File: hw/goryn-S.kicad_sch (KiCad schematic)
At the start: 2 parts, among them J2 Conn_01x34

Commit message: added DC-DC
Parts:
- added C8, C9: 22uF, AI6YP:C_0603_1608Metric, symbol AI6YP:C
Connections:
- net +3V3: now also C8.1, C9.1
- net GND: now also C8.2, C9.2
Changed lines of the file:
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@@
+    (stroke (width 0) (type default))
+  )
+  (wire (pts (xy 140 72) (xy 140 74))
     (stroke (width 0) (type default))
   )
@@
     (stroke (width 0) (type default))
   )
+  (wire (pts (xy 130 211) (xy 130 214))
+    (stroke (width 0) (type default))
+  )
   (wire (pts (xy 142 168) (xy 119 168))
     (stroke (width 0) (type default))
   )
+  (wire (pts (xy 130 216) (xy 130 218))
+    (stroke (width 0) (type default))
+  )
   (wire (pts (xy 113 136) (xy 113 132))
     (stroke (width 0) (type default))
@@
     (stroke (width 0) (type default))
   )
+  (wire (pts (xy 140 67) (xy 140 70))
+    (stroke (width 0) (type default))
+  )
   (wire (pts (xy 113 160) (xy 100 160))
     (stroke (width 0) (type default))
@@
     )
   )
+  (symbol (lib_id "AI6YP:C") (at 130 215 0) (unit 1)
+    (in_bom yes) (on_board yes) (dnp no)
+    (property "Reference" "C9" (at 131 214 0)
+      (effects (font (size 1 1)) (justify left))
+    )
+    (property "Value" "22uF" (at 131 216 0)
+      (effects (font (size 1 1)) (justify left))
+    )
+    (property "Footprint" "AI6YP:C_0603_1608Metric" (at 131 219 0)
+      (effects (font (size 1 1)) hide)
+    )
+    (property "Datasheet" "~" (at 130 215 0)
+      (effects (font (size 1 1)) hide)
+    )
+    (pin "1")
+    (pin "2")
+    (instances
+      (project "goryn"
+        (path "/745fe258-3c32-4527-ad01-ef9d3fd5a8f9/ce95a81f-e5e2-402d-b8f8-c902f6a2df69"
+          (reference "C9") (unit 1)
+        )
+      )
+    )
+  )
   (symbol (lib_id "AI6YP:GND") (at 103 116 90) (unit 1)
     (in_bom yes) (on_board yes) (dnp no) (fields_autoplaced)
@@
     )
   )
+  (symbol (lib_id "AI6YP:+3V3") (at 140 67 0) (unit 1)
+    (in_bom yes) (on_board yes) (dnp no) (fields_autoplaced)
+    (property "Reference" "#PWR0101" (at 140 69 0)
+      (effects (font (size 1 1)) hide)
+    )
+    (property "Value" "+3V3" (at 140 63.28 0)
+      (effects (font (size 1 1)))
+    )
+    (property "Footprint" "" (at 140 67 0)
+      (effects (font (size 1 1)) hide)
+    )
+    (property "Datasheet" "" (at 140 67 0)
+      (effects (font (size 1 1)) hide)
+    )
+    (pin "1")
+    (instances
+      (project "goryn"
+        (path "/745fe258-3c32-4527-ad01-ef9d3fd5a8f9/ce95a81f-e5e2-402d-b8f8-c902f6a2df69"
+          (reference "#PWR0101") (unit 1)
+        )
+      )
+    )
+  )
   (symbol (lib_id "AI6YP:GND") (at 103 80 90) (unit 1)
     (in_bom yes) (on_board yes) (dnp no) (fields_autoplaced)
@@
         (path "/745fe258-3c32-4527-ad01-ef9d3fd5a8f9/ce95a81f-e5e2-402d-b8f8-c902f6a2df69"
           (reference "#PWR018") (unit 1)
+        )
+      )
+    )
+  )
+  (symbol (lib_id "AI6YP:C") (at 140 71 0) (unit 1)
+    (in_bom yes) (on_board yes) (dnp no)
+    (property "Reference" "C8" (at 141 70 0)
+      (effects (font (size 1 1)) (justify left))
+    )
+    (property "Value" "22uF" (at 141 72 0)
+      (effects (font (size 1 1)) (justify left))
+    )
+    (property "Footprint" "AI6YP:C_0603_1608Metric" (at 141 75 0)
+      (effects (font (size 1 1)) hide)
+    )
+    (property "Datasheet" "~" (at 140 71 0)
+      (effects (font (size 1 1)) hide)
+    )
+    (pin "1")
+    (pin "2")
+    (instances
+      (project "goryn"
+        (path "/745fe258-3c32-4527-ad01-ef9d3fd5a8f9/ce95a81f-e5e2-402d-b8f8-c902f6a2df69"
+          (reference "C8") (unit 1)
+        )
+      )
+    )
+  )
+  (symbol (lib_id "AI6YP:+3V3") (at 130 211 0) (unit 1)
+    (in_bom yes) (on_board yes) (dnp no) (fields_autoplaced)
+    (property "Reference" "#PWR0103" (at 130 213 0)
+      (effects (font (size 1 1)) hide)
+    )
+    (property "Value" "+3V3" (at 130 207.28 0)
+      (effects (font (size 1 1)))
+    )
+    (property "Footprint" "" (at 130 211 0)
+      (effects (font (size 1 1)) hide)
+    )
+    (property "Datasheet" "" (at 130 211 0)
+      (effects (font (size 1 1)) hide)
+    )
+    (pin "1")
+    (instances
+      (project "goryn"
+        (path "/745fe258-3c32-4527-ad01-ef9d3fd5a8f9/ce95a81f-e5e2-402d-b8f8-c902f6a2df69"
+          (reference "#PWR0103") (unit 1)
         )
       )
@@
     )
   )
+  (symbol (lib_id "AI6YP:GND") (at 140 74 0) (unit 1)
+    (in_bom yes) (on_board yes) (dnp no) (fields_autoplaced)
+    (property "Reference" "#PWR0102" (at 140 78 0)
+      (effects (font (size 1 1)) hide)
+    )
+    (property "Value" "GND" (at 140 77.22 0)
+      (effects (font (size 1 1)))
+    )
+    (property "Footprint" "" (at 140 74 0)
+      (effects (font (size 1 1)) hide)
+    )
+    (property "Datasheet" "" (at 140 74 0)
+      (effects (font (size 1 1)) hide)
+    )
+    (pin "1")
+    (instances
+      (project "goryn"
+        (path "/745fe258-3c32-4527-ad01-ef9d3fd5a8f9/ce95a81f-e5e2-402d-b8f8-c902f6a2df69"
+          (reference "#PWR0102") (unit 1)
+        )
+      )
+    )
+  )
   (symbol (lib_id "AI6YP:GND") (at 137 108 270) (unit 1)
     (in_bom yes) (on_board yes) (dnp no) (fields_autoplaced)
@@
         )
       )
+    )
+  )
+  (symbol (lib_id "AI6YP:GND") (at 130 218 0) (unit 1)
+    (in_bom yes) (on_board yes) (dnp no) (fields_autoplaced)
+    (property "Reference" "#PWR0104" (at 130 222 0)
+      (effects (font (size 1 1)) hide)
+    )
+    (property "Value" "GND" (at 130 221.22 0)
+      (effects (font (size 1 1)))
+    )
+    (property "Footprint" "" (at 130 218 0)
+      (effects (font (size 1 1)) hide)
+    )
+    (property "Datasheet" "" (at 130 218 0)
+      (effects (font (size 1 1)) hide)
+    )
+    (pin "1")
+    (instances
+      (project "goryn"
+        (path "/745fe258-3c32-4527-ad01-ef9d3fd5a8f9/ce95a81f-e5e2-402d-b8f8-c902f6a2df69"
+          (reference "#PWR0104") (unit 1)
+        )
+      )

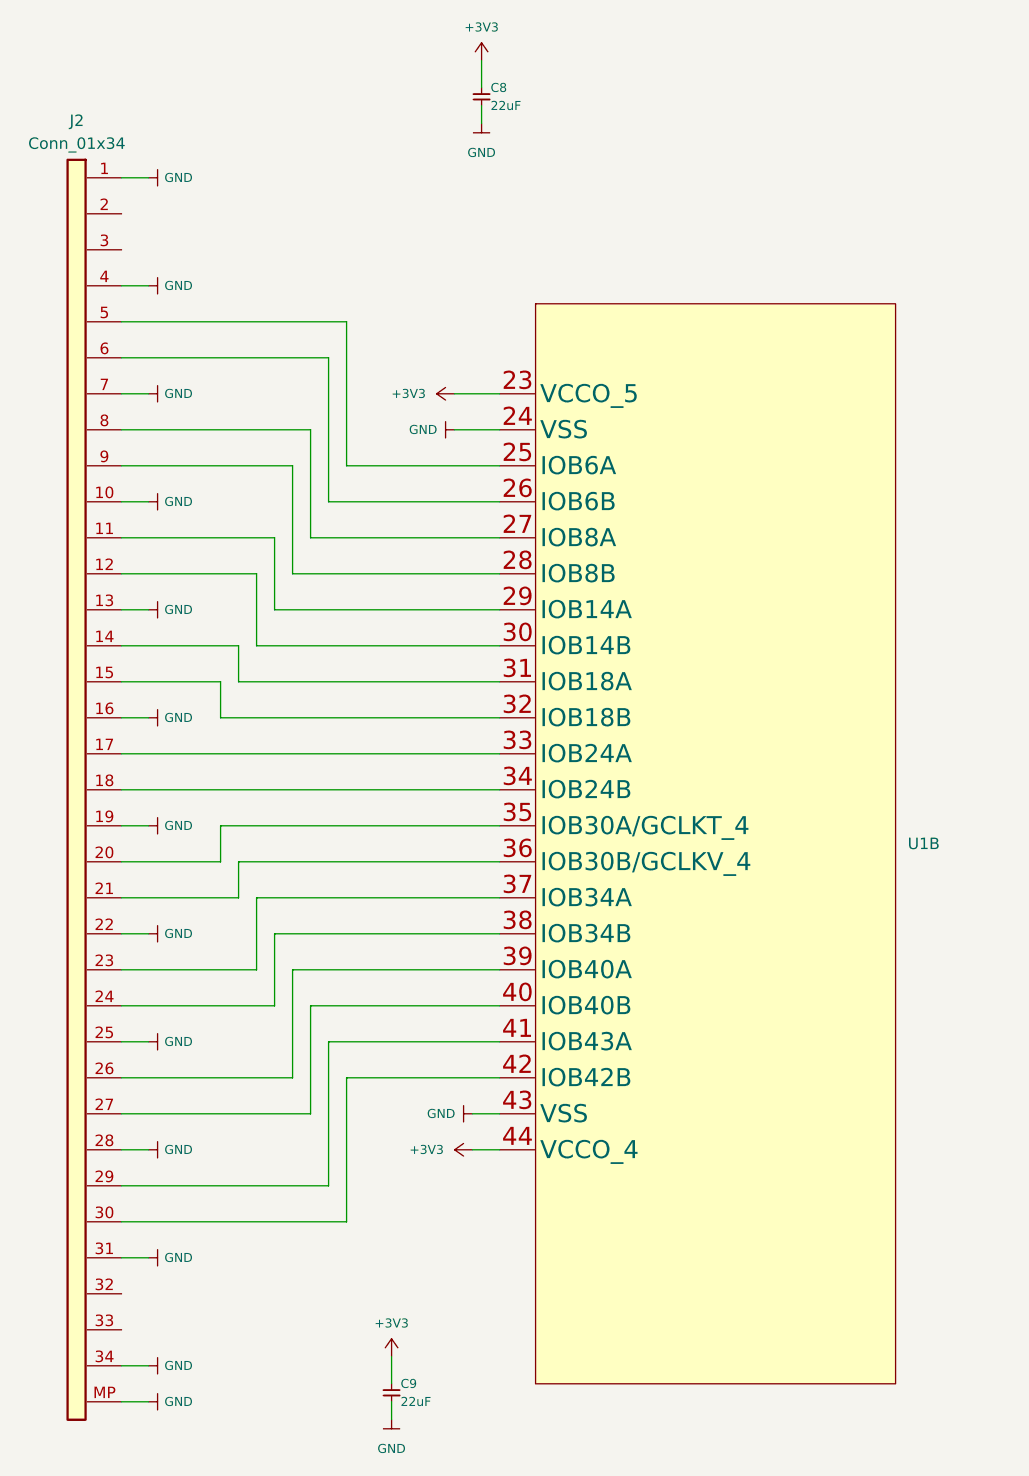
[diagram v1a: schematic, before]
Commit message: FFC34 -> FFC30
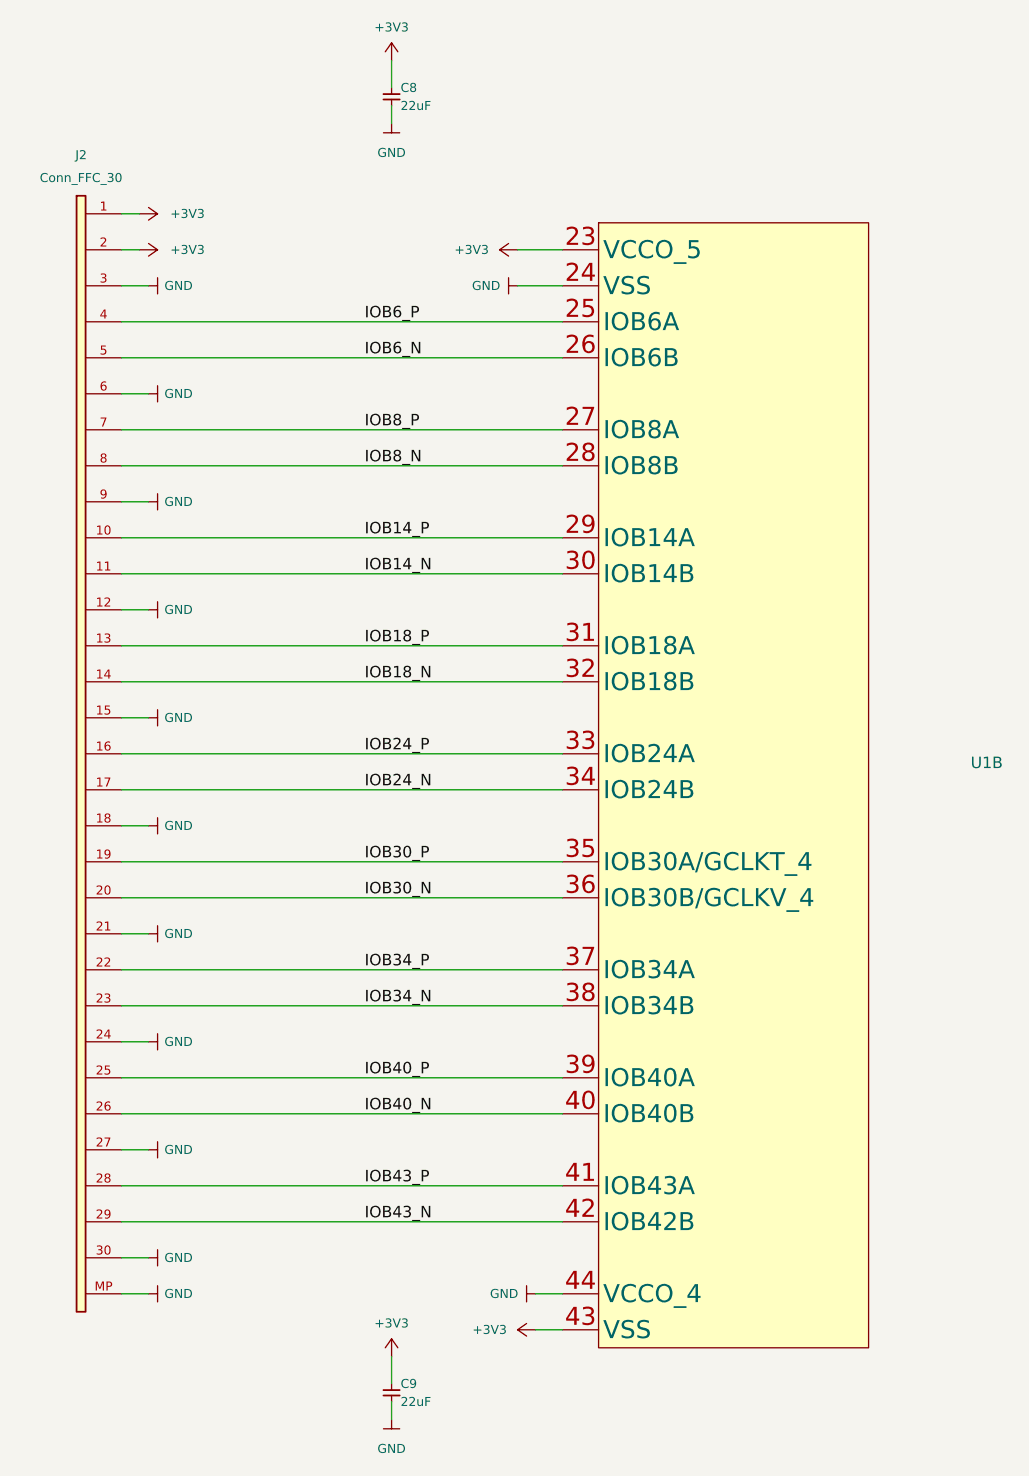
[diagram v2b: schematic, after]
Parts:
- removed J2: Conn_01x34, AI6YP:Hirose_FH12-34S-0.5SH_1x34-1MP_P0.50mm_Horizontal, symbol AI6YP:Conn_01x34
- added J2: Conn_FFC_30, AI6YP:Hirose_FH12-30S-0.5SH_1x30-1MP_P0.50mm_Horizontal, symbol AI6YP:Conn_FFC_30
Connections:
- net +3V3: now also U1.43 (VSS), J2.1 (Pin_1), J2.2 (Pin_2); no longer U1.44 (VCCO_4)
- net GND: now also U1.44 (VCCO_4), J2.12 (Pin_12), J2.15 (Pin_15), J2.18 (Pin_18), J2.21 (Pin_21), J2.24 (Pin_24), J2.27 (Pin_27), J2.3 (Pin_3), J2.30 (Pin_30), J2.6 (Pin_6), J2.9 (Pin_9), J2.MP (Pin_MP); no longer U1.43 (VSS)
- net IOB14_P: now reaches U1.29 (IOB14A)
- net IOB14_P: now also J2.10 (Pin_10)
- net IOB14_N: now reaches U1.30 (IOB14B)
- net IOB14_N: now also J2.11 (Pin_11)
- net IOB18_P: now reaches U1.31 (IOB18A)
- net IOB18_P: now also J2.13 (Pin_13)
- net IOB18_N: now reaches U1.32 (IOB18B)
- net IOB18_N: now also J2.14 (Pin_14)
- net IOB24_P: now reaches U1.33 (IOB24A)
- net IOB24_P: now also J2.16 (Pin_16)
- net IOB24_N: now reaches U1.34 (IOB24B)
- net IOB24_N: now also J2.17 (Pin_17)
- net IOB30_P: now reaches U1.35 (IOB30A/GCLKT_4)
- net IOB30_P: now also J2.19 (Pin_19)
- net IOB30_N: now reaches U1.36 (IOB30B/GCLKV_4)
- net IOB30_N: now also J2.20 (Pin_20)
- net IOB34_P: now reaches U1.37 (IOB34A)
- net IOB34_P: now also J2.22 (Pin_22)
- net IOB34_N: now reaches U1.38 (IOB34B)
- net IOB34_N: now also J2.23 (Pin_23)
- net IOB40_P: now reaches U1.39 (IOB40A)
- net IOB40_P: now also J2.25 (Pin_25)
- net IOB40_N: now reaches U1.40 (IOB40B)
- net IOB40_N: now also J2.26 (Pin_26)
- net IOB43_P: now reaches U1.41 (IOB43A)
- net IOB43_P: now also J2.28 (Pin_28)
- net IOB43_N: now reaches U1.42 (IOB42B)
- net IOB43_N: now also J2.29 (Pin_29)
- net IOB6_P: now reaches U1.25 (IOB6A)
- net IOB6_P: now also J2.4 (Pin_4)
- net IOB6_N: now reaches U1.26 (IOB6B)
- net IOB6_N: now also J2.5 (Pin_5)
- net IOB8_P: now reaches U1.27 (IOB8A)
- net IOB8_P: now also J2.7 (Pin_7)
- net IOB8_N: now reaches U1.28 (IOB8B)
- net IOB8_N: now also J2.8 (Pin_8)
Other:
- moved on the sheet: C8, U1B

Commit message: happy kicad 8
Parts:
- added H2: MountingHole_M3, AI6YP:MountingHole_3.2mm_M3_Pad_Via, symbol AI6YP:MountingHole_M3
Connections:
- net +3V3: now also J2.30 (Pin_30), U1.44 (VCCO_4); no longer J2.2 (Pin_2), U1.43 (VSS)
- net GND: now also J2.11 (Pin_11), J2.14 (Pin_14), J2.17 (Pin_17), J2.2 (Pin_2), J2.20 (Pin_20), J2.23 (Pin_23), J2.26 (Pin_26), J2.29 (Pin_29), J2.5 (Pin_5), J2.8 (Pin_8), U1.43 (VSS), H2.1; no longer J2.12 (Pin_12), J2.15 (Pin_15), J2.18 (Pin_18), J2.21 (Pin_21), J2.24 (Pin_24), J2.27 (Pin_27), J2.3 (Pin_3), J2.30 (Pin_30), J2.6 (Pin_6), J2.9 (Pin_9), U1.44 (VCCO_4)
- net IOB14_N: now also J2.10 (Pin_10); no longer J2.11 (Pin_11)
- net IOB14_P: now also J2.9 (Pin_9); no longer J2.10 (Pin_10)
- net IOB18_N: now also J2.13 (Pin_13); no longer J2.14 (Pin_14)
- net IOB18_P: now also J2.12 (Pin_12); no longer J2.13 (Pin_13)
- net IOB24_N: now also J2.16 (Pin_16); no longer J2.17 (Pin_17)
- net IOB24_P: now also J2.15 (Pin_15); no longer J2.16 (Pin_16)
- net IOB30_N: now also J2.19 (Pin_19); no longer J2.20 (Pin_20)
- net IOB30_P: now also J2.18 (Pin_18); no longer J2.19 (Pin_19)
- net IOB34_N: now also J2.22 (Pin_22); no longer J2.23 (Pin_23)
- net IOB34_P: now also J2.21 (Pin_21); no longer J2.22 (Pin_22)
- net IOB40_N: now also J2.25 (Pin_25); no longer J2.26 (Pin_26)
- net IOB40_P: now also J2.24 (Pin_24); no longer J2.25 (Pin_25)
- net IOB43_N: now also J2.28 (Pin_28); no longer J2.29 (Pin_29)
- net IOB43_P: now also J2.27 (Pin_27); no longer J2.28 (Pin_28)
- net IOB6_N: now also J2.4 (Pin_4); no longer J2.5 (Pin_5)
- net IOB6_P: now also J2.3 (Pin_3); no longer J2.4 (Pin_4)
- net IOB8_N: now also J2.7 (Pin_7); no longer J2.8 (Pin_8)
- net IOB8_P: now also J2.6 (Pin_6); no longer J2.7 (Pin_7)
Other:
- moved on the sheet: C8, C9, J2, U1B

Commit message: finished routing
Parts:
- removed H2: MountingHole_M3, AI6YP:MountingHole_3.2mm_M3_Pad_Via, symbol AI6YP:MountingHole_M3
- added C1, C32, C42: 22uF, AI6YP:C_0603_1608Metric, symbol AI6YP:C
- added C31, C41: 10uF, AI6YP:C_0603_1608Metric, symbol AI6YP:C
- added J6: USB_C_Receptacle_USB2.0_16P, AI6YP:USB_C_Receptacle_GCT_USB4105-xx-A_16P_TopMnt_Horizontal, symbol AI6YP:USB_C_Receptacle_USB2.0_16P
- added L31, L41: 2.2uH, AI6YP:L_0805_2012Metric_Pad1.05x1.20mm_HandSolder, symbol AI6YP:L
- added R10, R11: 5.1K, AI6YP:R_0603_1608Metric, symbol AI6YP:R
- added R12, R13: 0R, AI6YP:R_0603_1608Metric, symbol AI6YP:R
- added R31: 68K, AI6YP:R_0603_1608Metric, symbol AI6YP:R
- added R32, R42: 15K, AI6YP:R_0603_1608Metric, symbol AI6YP:R
- added R41: 10K, AI6YP:R_0603_1608Metric, symbol AI6YP:R
- added U3, U4: MT3520B, AI6YP:SOT-23-5, symbol AI6YP:MT3520B
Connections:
- net +3V3: now also C32.1, L31.2, R31.1
- net GND: now also C1.2, C31.2, C32.2, C41.2, C42.2, J6.A1 (GND), J6.A12 (GND), J6.B1 (GND), J6.B12 (GND), J6.S1 (SHIELD), R10.2, R11.2, R32.2, R42.2, U3.2 (GND), U4.2 (GND)
- net IOB6_N: now also R13.2
- net IOB6_P: now also R12.2
- net IOB43_N: no longer names the net of J2.28 (Pin_28), U1.42 (IOB42B)
- net IOB43_P: no longer names the net of J2.27 (Pin_27), U1.41 (IOB43A)
- new net: R41.2, R42.1, U4.5 (FB)
- new net: J6.B5 (CC2), R11.1
- new net: J6.A7 (D-), J6.B7 (D-), R12.1
- new net: L41.1, U4.3 (SW)
- new net: J6.A5 (CC1), R10.1
- new net: J6.A6 (D+), J6.B6 (D+), R13.1
- new net: R31.2, R32.1, U3.5 (FB)
- new net: L31.1, U3.3 (SW)
- new net +1V0: C1.1, C42.1, L41.2, R41.1
- new net +5V: C31.1, C41.1, J6.A4 (VBUS), J6.A9 (VBUS), J6.B4 (VBUS), J6.B9 (VBUS), U3.1 (EN), U3.4 (VIN), U4.1 (EN), U4.4 (VIN)
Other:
- moved on the sheet: C8, C9, J2, U1B

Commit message: v1.0.0
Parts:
- U1: footprint AI6YP:QFN-88-10x10mm-P0.4mm-EP6.74x6.74mm -> AI6YP:GIWIN-QFN-88-10x10mm-P0.4mm-EP6.74x6.74mm
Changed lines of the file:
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@@
 			)
 		)
-		(property "Footprint" "AI6YP:QFN-88-10x10mm-P0.4mm-EP6.74x6.74mm"
+		(property "Footprint" "AI6YP:GIWIN-QFN-88-10x10mm-P0.4mm-EP6.74x6.74mm"
 			(at 180 87 0)
 			(effects
